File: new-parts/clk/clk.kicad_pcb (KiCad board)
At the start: 2 copper layers, 47 x 43.2 mm, 10 parts, among them J1 Conn_02x02_Odd_Even, J2 Conn_01x08, K1 J104D2C12VDC.15S, K2 J104D2C12VDC.15S

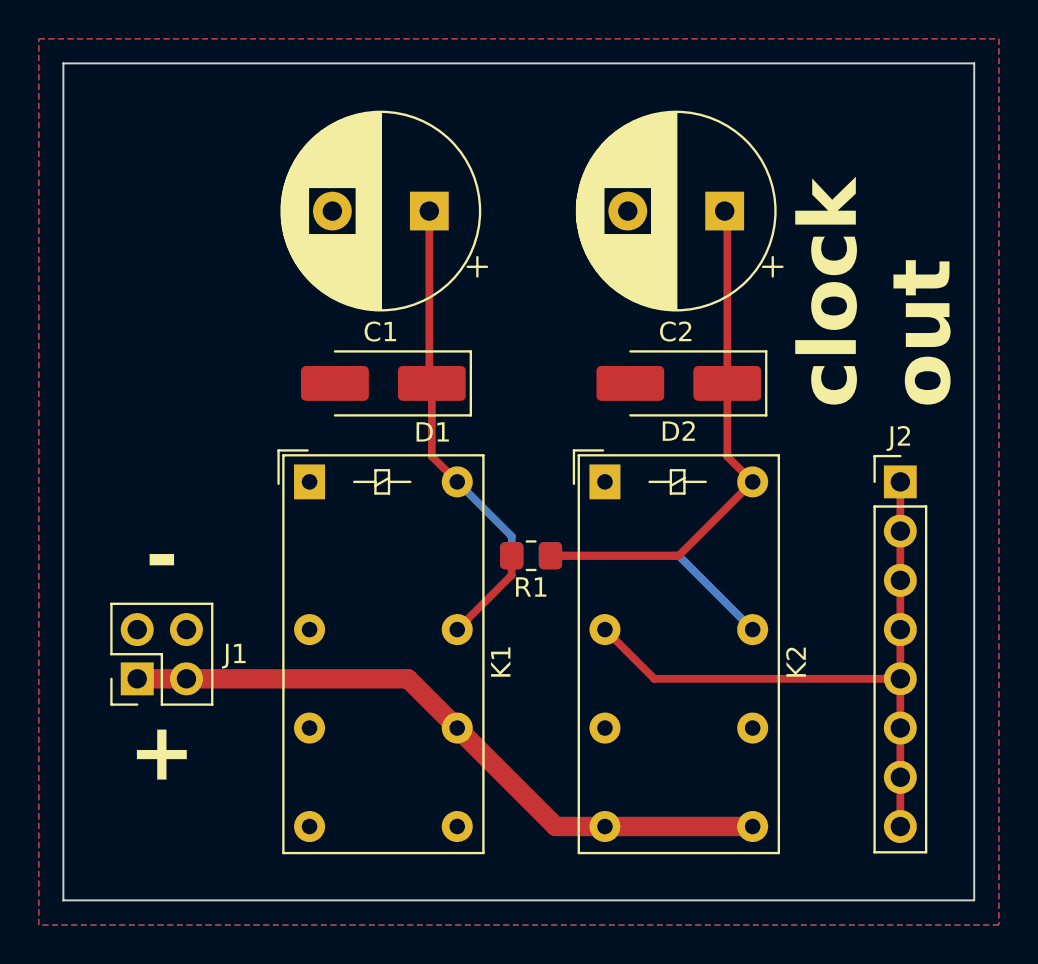
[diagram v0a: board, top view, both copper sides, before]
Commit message: clk: Add trimming resistors.
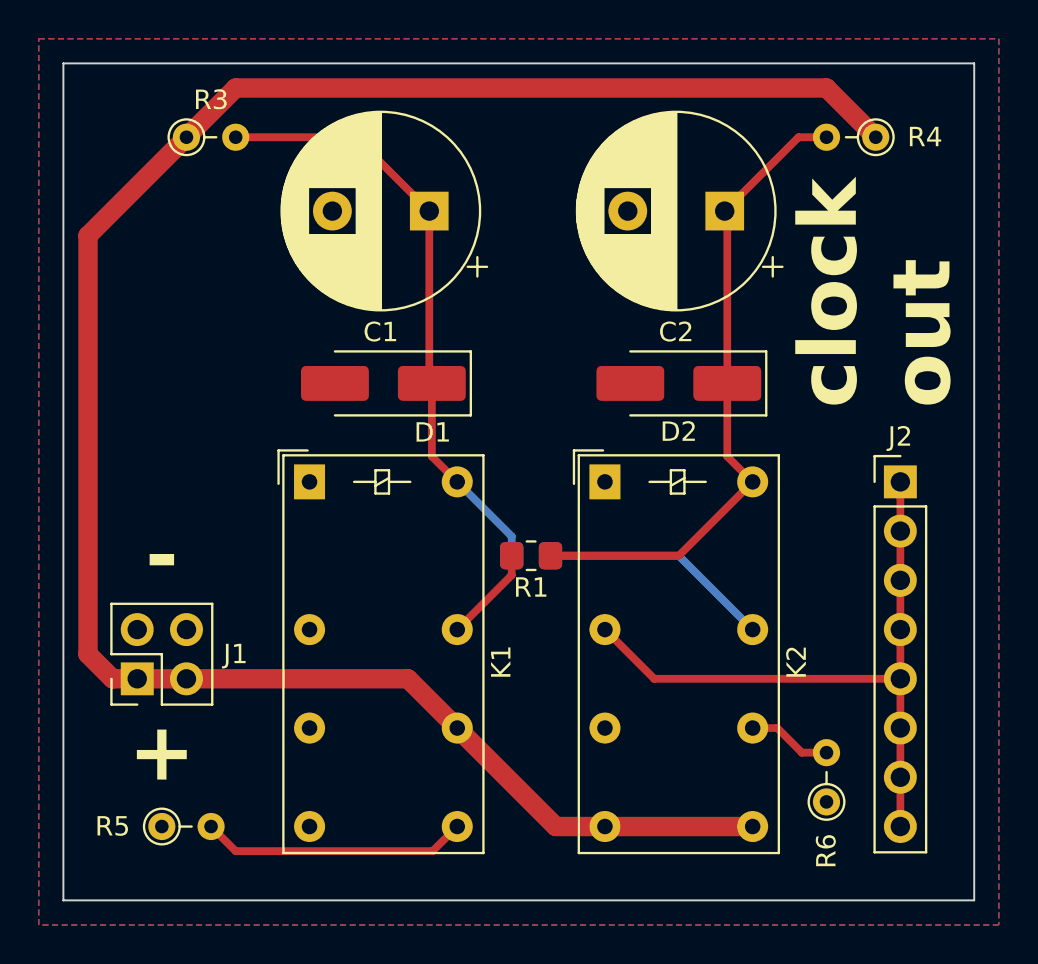
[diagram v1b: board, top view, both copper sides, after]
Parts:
- added R3: 15kR, Resistor_THT:R_Axial_DIN0204_L3.6mm_D1.6mm_P2.54mm_Vertical, F.Cu at (123.2, 58.4)
- added R4: 15kR, Resistor_THT:R_Axial_DIN0204_L3.6mm_D1.6mm_P2.54mm_Vertical, F.Cu at (158.8, 58.4)
- added R5: 15kR, Resistor_THT:R_Axial_DIN0204_L3.6mm_D1.6mm_P2.54mm_Vertical, F.Cu at (121.9, 94.0)
- added R6: 15kR, Resistor_THT:R_Axial_DIN0204_L3.6mm_D1.6mm_P2.54mm_Vertical, F.Cu at (156.2, 92.7)
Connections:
- K1 pad 24: unconnected-(K1-Pad24) -> Net-(K1-Pad24)
- K2 pad 22: unconnected-(K2-Pad22) -> Net-(K2-Pad22)
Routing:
- net VCC: track 34.9 -> 104.4 mm
- net Net-(K1-Pad24): track 0.00 -> 13.8 mm
- net Net-(D1-A1): track 19.5 -> 31.1 mm
- net Net-(D2-A1): track 26.6 -> 33.4 mm
- net Net-(K2-Pad22): track 0.00 -> 4.34 mm
